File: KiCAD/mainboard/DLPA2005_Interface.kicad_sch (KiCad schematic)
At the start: 37 parts, among them J14 Conn_01x04_Pin, U24 DLPA2005ERSLT

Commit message: BGA layout cont
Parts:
- R83: footprint RC0805FR-0730R1L:RESC2012X60N -> RESC2012X60N
- TP2, TP22, TP35, TP36, TP38: footprint (none) -> TestPoint:TestPoint_Pad_D1.5mm
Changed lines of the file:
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@@
 			)
 		)
-		(property "Footprint" ""
+		(property "Footprint" "TestPoint:TestPoint_Pad_D1.5mm"
 			(at 128.27 30.48 0)
 			(effects
@@
 			)
 		)
-		(property "Footprint" ""
+		(property "Footprint" "TestPoint:TestPoint_Pad_D1.5mm"
 			(at 43.18 63.5 0)
 			(effects
@@
 			)
 		)
-		(property "Footprint" ""
+		(property "Footprint" "TestPoint:TestPoint_Pad_D1.5mm"
 			(at 191.77 54.61 0)
 			(effects
@@
 			)
 		)
-		(property "Footprint" "RC0805FR-0730R1L:RESC2012X60N"
+		(property "Footprint" "RESC2012X60N"
 			(at 90.17 25.4 0)
 			(effects
@@
 			)
 		)
-		(property "Footprint" ""
+		(property "Footprint" "TestPoint:TestPoint_Pad_D1.5mm"
 			(at 91.44 160.02 0)
 			(effects
@@
 			)
 		)
-		(property "Footprint" ""
+		(property "Footprint" "TestPoint:TestPoint_Pad_D1.5mm"
 			(at 130.81 30.48 0)
 			(effects

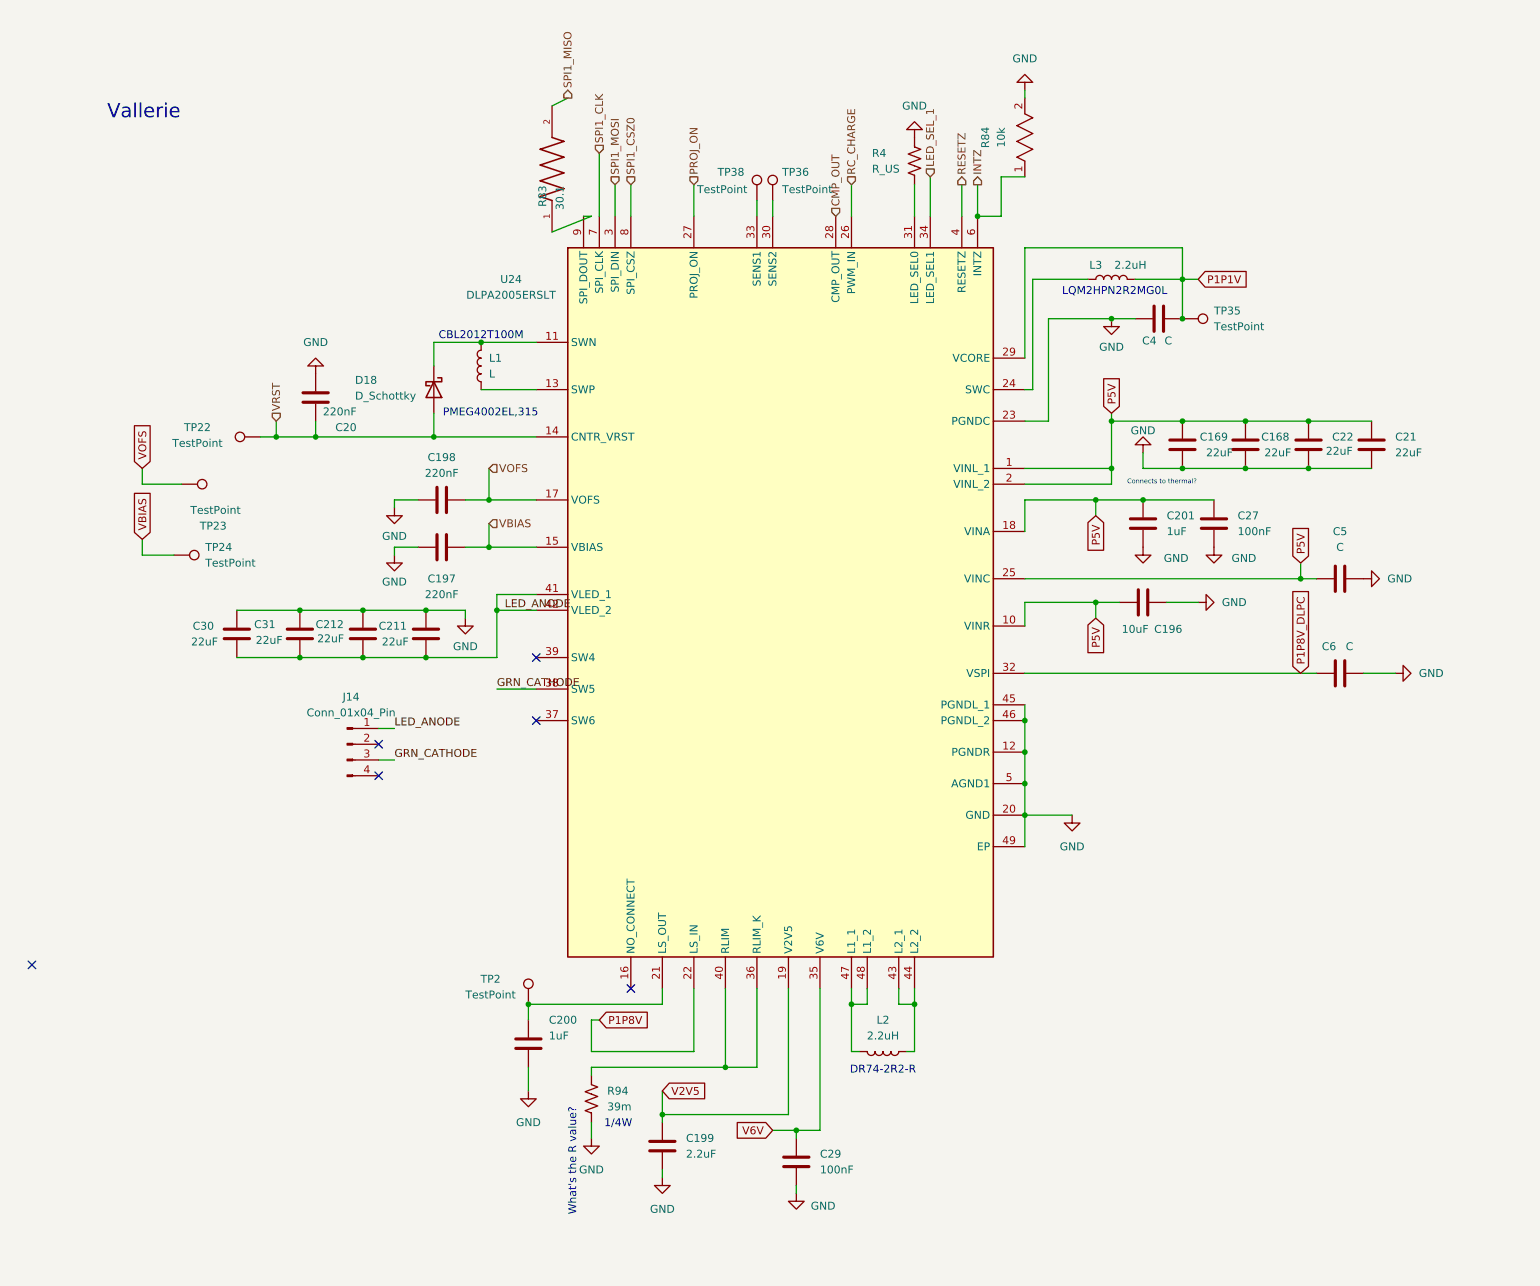
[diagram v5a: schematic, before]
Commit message: updated footprint to new IEEE folder
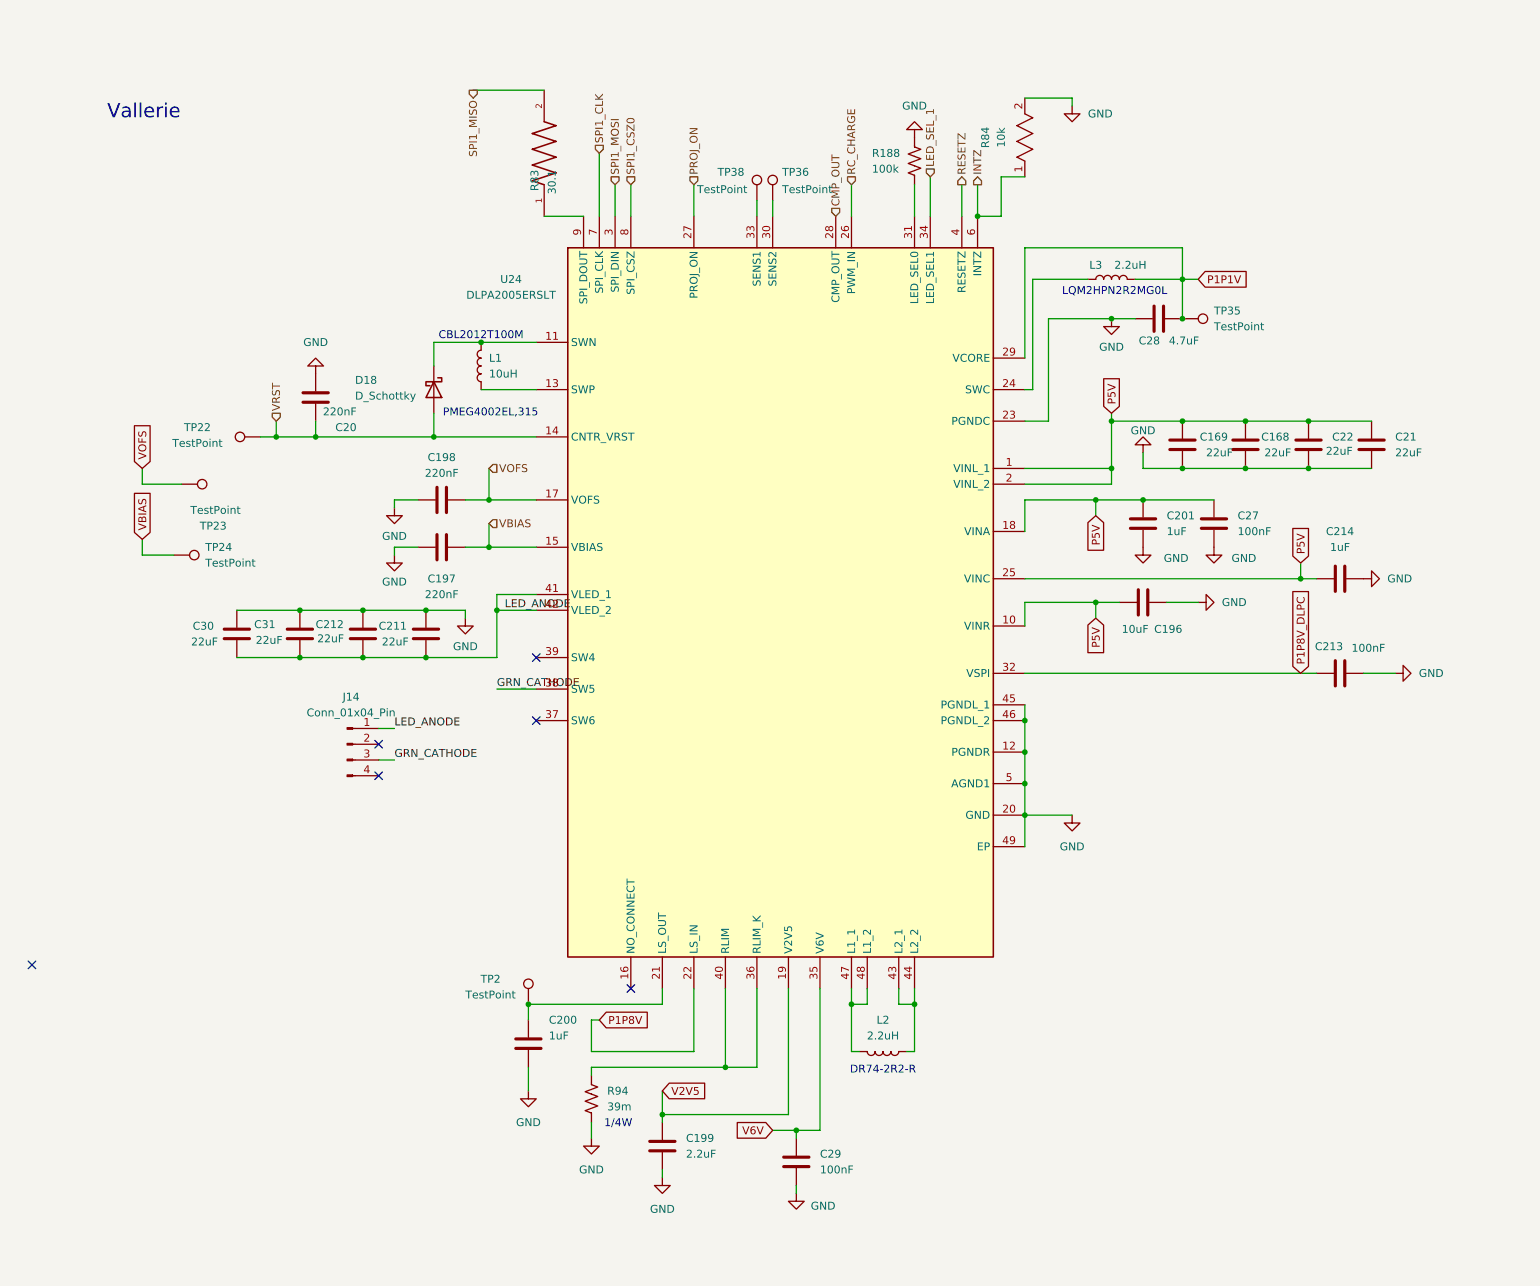
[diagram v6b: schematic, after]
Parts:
- C168, C169, C21, C211, C212, C22, C30, C31: footprint Capacitor_SMD:C_0603_1608Metric -> tp_library:CAPC1608X100N
- C199, C200, C201: footprint (none) -> tp_library:CAPC2012X135N
- C213: renamed from C6; value C -> 100nF
- C214: renamed from C5; value C -> 1uF; footprint (none) -> tp_library:CAPC2012X135N
- C28: renamed from C4; value C -> 4.7uF
- D18: footprint (none) -> tp_library:DIO_PESD5V0S1UL_315
- L1: value L -> 10uH; footprint (none) -> tp_library:INDC2012X100N
- L2, L3: footprint (none) -> tp_library:INDC2520X100N
- R188: renamed from R4; value R_US -> 100k
- R83: footprint RESC2012X60N -> tp_library:RESC1005X40N
- R94: footprint (none) -> tp_library:RESC1608X60N
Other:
- note removed: "Connects to thermal?"
- note removed: "What's the R value?"
- moved on the sheet: R83

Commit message: refactor
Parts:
- removed C213: 100nF, symbol Device:C
- removed C214: 1uF, tp_library:CAPC2012X135N, symbol Device:C
- removed C28: 4.7uF, symbol Device:C
- removed R188: 100k, symbol Device:R_US
- added C4, C5, C6: C, symbol Device:C
- added R4: R_US, symbol Device:R_US
- C168, C169, C21, C211, C212, C22, C30, C31: footprint tp_library:CAPC1608X100N -> Capacitor_SMD:C_0603_1608Metric
- C199, C200, C201: footprint tp_library:CAPC2012X135N -> (none)
- D18: footprint tp_library:DIO_PESD5V0S1UL_315 -> (none)
- L1: value 10uH -> L; footprint tp_library:INDC2012X100N -> (none)
- L2, L3: footprint tp_library:INDC2520X100N -> (none)
- R83: footprint tp_library:RESC1005X40N -> RESC2012X60N
- R94: footprint tp_library:RESC1608X60N -> (none)
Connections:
- net GND: now also C4.1, C5.2, C6.2, R4.1
- net P1P1V: now also C4.2
- net P1P8V_DLPC: now also C6.1
- net P5V: now also C5.1
- net at U24.31 (LED_SEL0): now also R4.2
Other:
- note added: "Connects to thermal?"
- note added: "What's the R value?"

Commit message: schematic chagnesS
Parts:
- removed C4, C5, C6: C, symbol Device:C
- removed R4: R_US, symbol Device:R_US
- added C213: 100nF, tp_library:CAP_CL05_SAM, symbol Device:C
- added C214: 1uF, tp_library:CAPC2012X135N, symbol Device:C
- added C28: 4.7uF, tp_library:CAP_CL05_SAM, symbol Device:C
- added R188: 100k, Resistor_SMD:R_0402_1005Metric, symbol Device:R_US
- C168, C169, C21, C211, C212, C22, C30, C31: footprint Capacitor_SMD:C_0603_1608Metric -> tp_library:CAPC1608X100N
- C196, C197, C20: footprint (none) -> Capacitor_SMD:C_0603_1608Metric_Pad1.08x0.95mm_HandSolder
- C198: footprint (none) -> C1608X5R1A226M080AC
- C199, C200, C201: footprint (none) -> tp_library:CAPC2012X135N
- C27, C29: footprint (none) -> tp_library:CAP_CL05_SAM
- D18: footprint (none) -> tp_library:DIO_PESD5V0S1UL_315
- L1: value L -> 10uH; footprint (none) -> tp_library:INDC2012X100N
- L2, L3: footprint (none) -> tp_library:INDC2520X100N
- R83: footprint RESC2012X60N -> tp_library:RESC1005X40N
- R94: footprint (none) -> tp_library:RESC1608X60N
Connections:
- net GND: now also C213.2, C214.2, C28.1, R188.1
- net P1P1V: now also C28.2
- net P1P8V_DLPC: now also C213.1
- net P5V: now also C214.1
- net at U24.31 (LED_SEL0): now also R188.2
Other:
- note removed: "Connects to thermal?"
- note removed: "What's the R value?"
